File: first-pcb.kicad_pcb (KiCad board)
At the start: 2 copper layers, 88.9 x 53.3 mm, 12 parts, among them K1 my_connector, P1 10k, Q1 BC547, U1 LM358

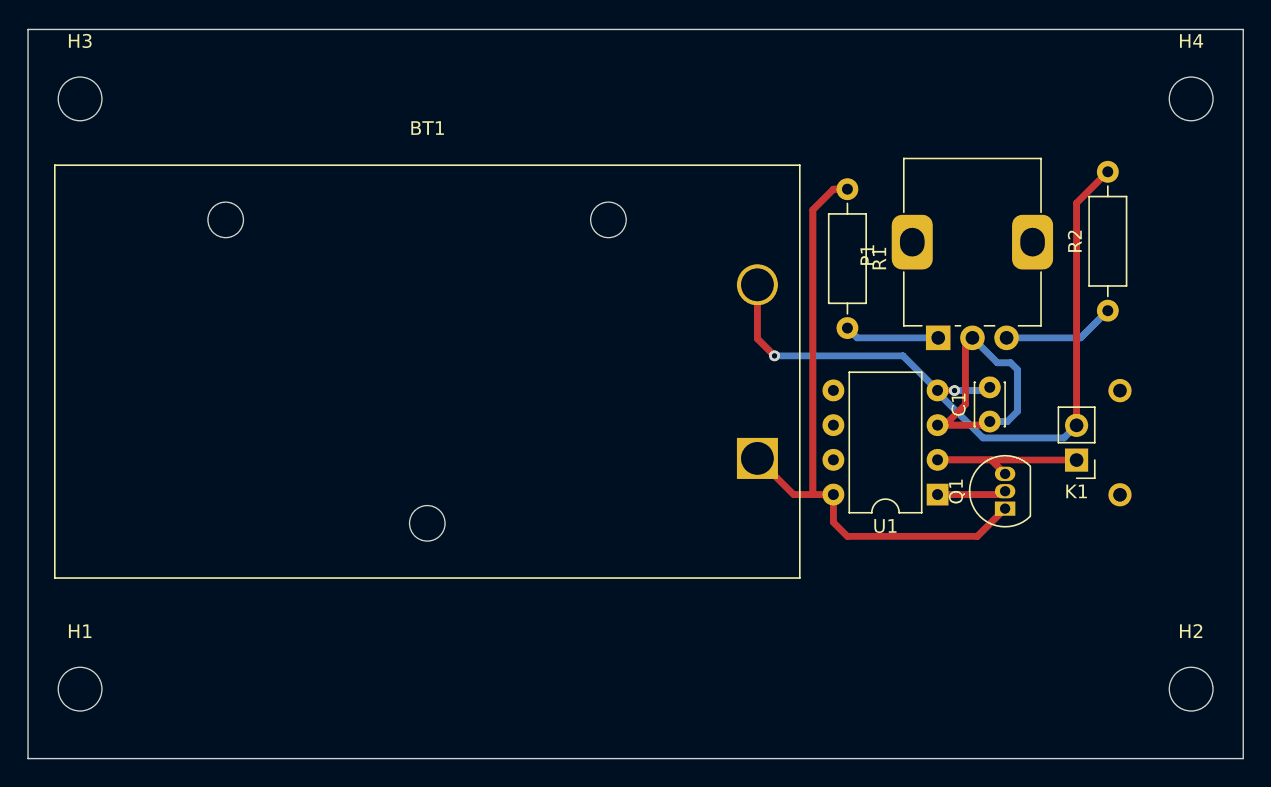
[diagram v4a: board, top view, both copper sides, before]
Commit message: Mounting Hole Footprint Change
Changing mounting hole footprint to a pad to have the front and back connected.
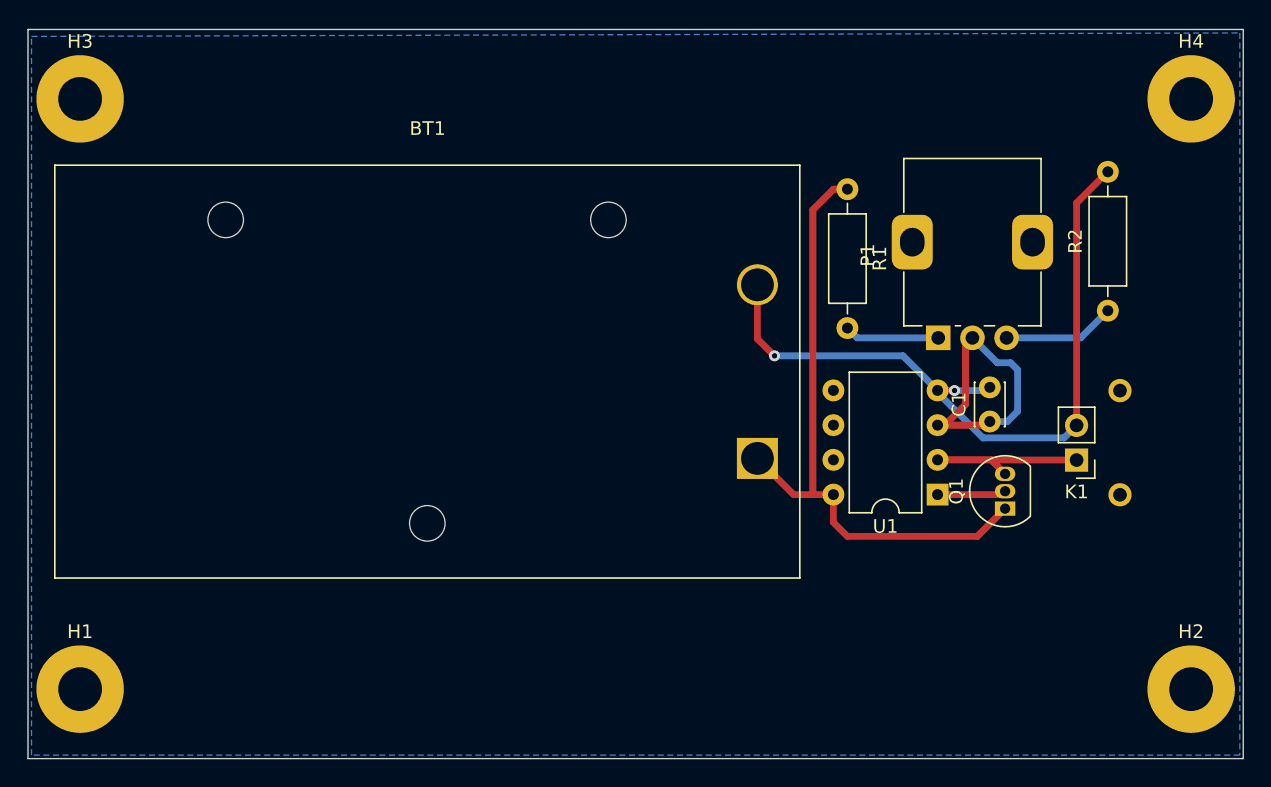
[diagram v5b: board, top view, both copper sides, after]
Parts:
- H1, H2, H3, H4: footprint MountingHole:MountingHole_3.2mm_M3 -> MountingHole:MountingHole_3.2mm_M3_Pad
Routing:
- added copper zone on B.Cu, net GND
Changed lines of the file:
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@@
     )
   )
-  (footprint "MountingHole:MountingHole_3.2mm_M3" (layer "F.Cu")
+  (footprint "MountingHole:MountingHole_3.2mm_M3_Pad" (layer "F.Cu")
     (at 86.36 76.2)
-    (descr "Mounting Hole 3.2mm, no annular, M3")
-    (tags "mounting hole 3.2mm no annular m3")
+    (descr "Mounting Hole 3.2mm, M3")
+    (tags "mounting hole 3.2mm m3")
     (property "Sheetfile" "first-pcb.kicad_sch")
     (property "Sheetname" "")
@@
     (fp_circle (center 0 0) (end 3.2 0) (layer "Cmts.User") (width 0.15) (fill none))
     (fp_circle (center 0 0) (end 3.45 0) (layer "F.CrtYd") (width 0.05) (fill none))
-    (pad "" np_thru_hole circle (at 0 0) (size 3.2 3.2) (drill 3.2) (layers *.Cu *.Mask))
-  )
-  (footprint "MountingHole:MountingHole_3.2mm_M3" (layer "F.Cu")
+    (pad "1" thru_hole circle (at 0 0) (size 6.4 6.4) (drill 3.2) (layers *.Cu *.Mask)
+      (net 4 "GND") (pinfunction "1") (pintype "input"))
+  )
+  (footprint "MountingHole:MountingHole_3.2mm_M3_Pad" (layer "F.Cu")
     (at 86.36 119.38)
-    (descr "Mounting Hole 3.2mm, no annular, M3")
-    (tags "mounting hole 3.2mm no annular m3")
+    (descr "Mounting Hole 3.2mm, M3")
+    (tags "mounting hole 3.2mm m3")
     (property "Sheetfile" "first-pcb.kicad_sch")
     (property "Sheetname" "")
@@
     (fp_circle (center 0 0) (end 3.2 0) (layer "Cmts.User") (width 0.15) (fill none))
     (fp_circle (center 0 0) (end 3.45 0) (layer "F.CrtYd") (width 0.05) (fill none))
-    (pad "" np_thru_hole circle (at 0 0) (size 3.2 3.2) (drill 3.2) (layers *.Cu *.Mask))
+    (pad "1" thru_hole circle (at 0 0) (size 6.4 6.4) (drill 3.2) (layers *.Cu *.Mask)
+      (net 4 "GND") (pinfunction "1") (pintype "input"))
   )
   (footprint "Battery:BatteryHolder_Eagle_12BH611-GR" (layer "F.Cu")
@@
     )
   )
-  (footprint "MountingHole:MountingHole_3.2mm_M3" (layer "F.Cu")
+  (footprint "MountingHole:MountingHole_3.2mm_M3_Pad" (layer "F.Cu")
     (at 167.64 119.38)
-    (descr "Mounting Hole 3.2mm, no annular, M3")
-    (tags "mounting hole 3.2mm no annular m3")
+    (descr "Mounting Hole 3.2mm, M3")
+    (tags "mounting hole 3.2mm m3")
     (property "Sheetfile" "first-pcb.kicad_sch")
     (property "Sheetname" "")
@@
     (fp_circle (center 0 0) (end 3.2 0) (layer "Cmts.User") (width 0.15) (fill none))
     (fp_circle (center 0 0) (end 3.45 0) (layer "F.CrtYd") (width 0.05) (fill none))
-    (pad "" np_thru_hole circle (at 0 0) (size 3.2 3.2) (drill 3.2) (layers *.Cu *.Mask))
+    (pad "1" thru_hole circle (at 0 0) (size 6.4 6.4) (drill 3.2) (layers *.Cu *.Mask)
+      (net 4 "GND") (pinfunction "1") (pintype "input"))
   )
   (footprint "Capacitor_THT:C_Disc_D3.0mm_W2.0mm_P2.50mm" (layer "F.Cu")
@@
     )
   )
-  (footprint "MountingHole:MountingHole_3.2mm_M3" (layer "F.Cu")
+  (footprint "MountingHole:MountingHole_3.2mm_M3_Pad" (layer "F.Cu")
     (at 167.64 76.2)
-    (descr "Mounting Hole 3.2mm, no annular, M3")
-    (tags "mounting hole 3.2mm no annular m3")
+    (descr "Mounting Hole 3.2mm, M3")
+    (tags "mounting hole 3.2mm m3")
     (property "Sheetfile" "first-pcb.kicad_sch")
     (property "Sheetname" "")
@@
     (fp_circle (center 0 0) (end 3.2 0) (layer "Cmts.User") (width 0.15) (fill none))
     (fp_circle (center 0 0) (end 3.45 0) (layer "F.CrtYd") (width 0.05) (fill none))
-    (pad "" np_thru_hole circle (at 0 0) (size 3.2 3.2) (drill 3.2) (layers *.Cu *.Mask))
+    (pad "1" thru_hole circle (at 0 0) (size 6.4 6.4) (drill 3.2) (layers *.Cu *.Mask)
+      (net 4 "GND") (pinfunction "1") (pintype "input"))
   )
   (gr_rect (start 82.55 124.46) (end 171.45 71.12) (layer "Edge.Cuts") (width 0.1) (fill none))
@@
   (segment (start 153.786 105.146) (end 154.03 104.902) (width 0.5) (layer "F.Cu") (net 10))
   (segment (start 149.088 105.146) (end 153.786 105.146) (width 0.5) (layer "F.Cu") (net 10))
+  (zone (net 4) (net_name "GND") (layer "B.Cu") (hatch none 0.508)
+    (connect_pads (clearance 0.508))
+    (min_thickness 0.254) (filled_areas_thickness no)
+    (fill yes (thermal_gap 0.508) (thermal_bridge_width 0.508))
+    (polygon
+      (pts
+        (xy 171.196 124.206)
+        (xy 82.804 124.206)
+        (xy 82.804 71.628)
+        (xy 171.196 71.374)
+      )
+    )
+  )
 )

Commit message: Dimensions/Silkscreen Icons/Text
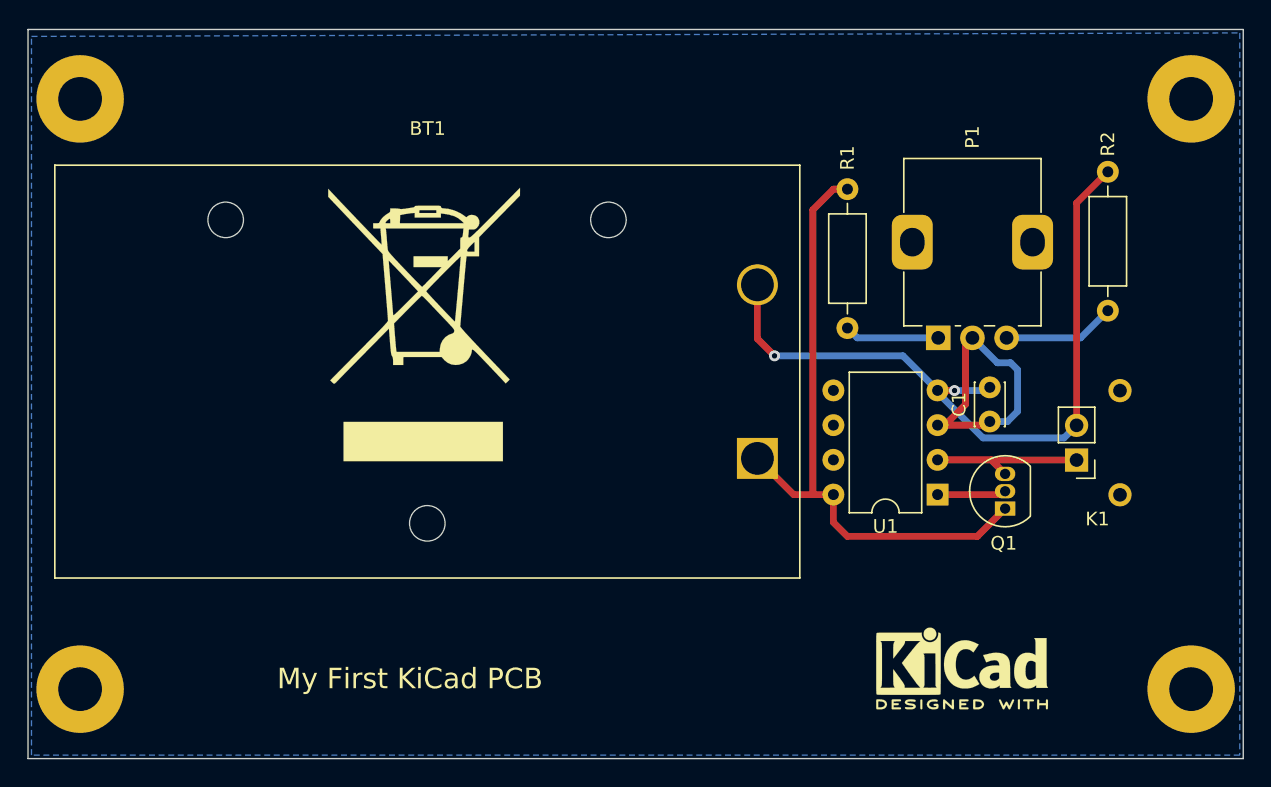
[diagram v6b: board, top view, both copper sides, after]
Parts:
- added REF**: WEEE-Logo_14x20mm_SilkScreen, Symbol:WEEE-Logo_14x20mm_SilkScreen, F.Cu at (111.5, 92.7)
- added REF**: KiCad-Logo2_5mm_SilkScreen, Symbol:KiCad-Logo2_5mm_SilkScreen, F.Cu at (150.9, 117.9)
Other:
- board text added: "My First KiCad PCB"
